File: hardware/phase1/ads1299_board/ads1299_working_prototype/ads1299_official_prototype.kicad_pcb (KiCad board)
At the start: 4 copper layers, 98 parts, among them Con1-32 PinSocket_2x16_P2.54mm_Vertic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, J3 TSM-110-01-T-DV-P-TR, J6 36PIN_IDC, U1 ADS1299IPAG, U10 24AA256-I/ST, U11 SOIC127P599X175-8N, U4 OPA376

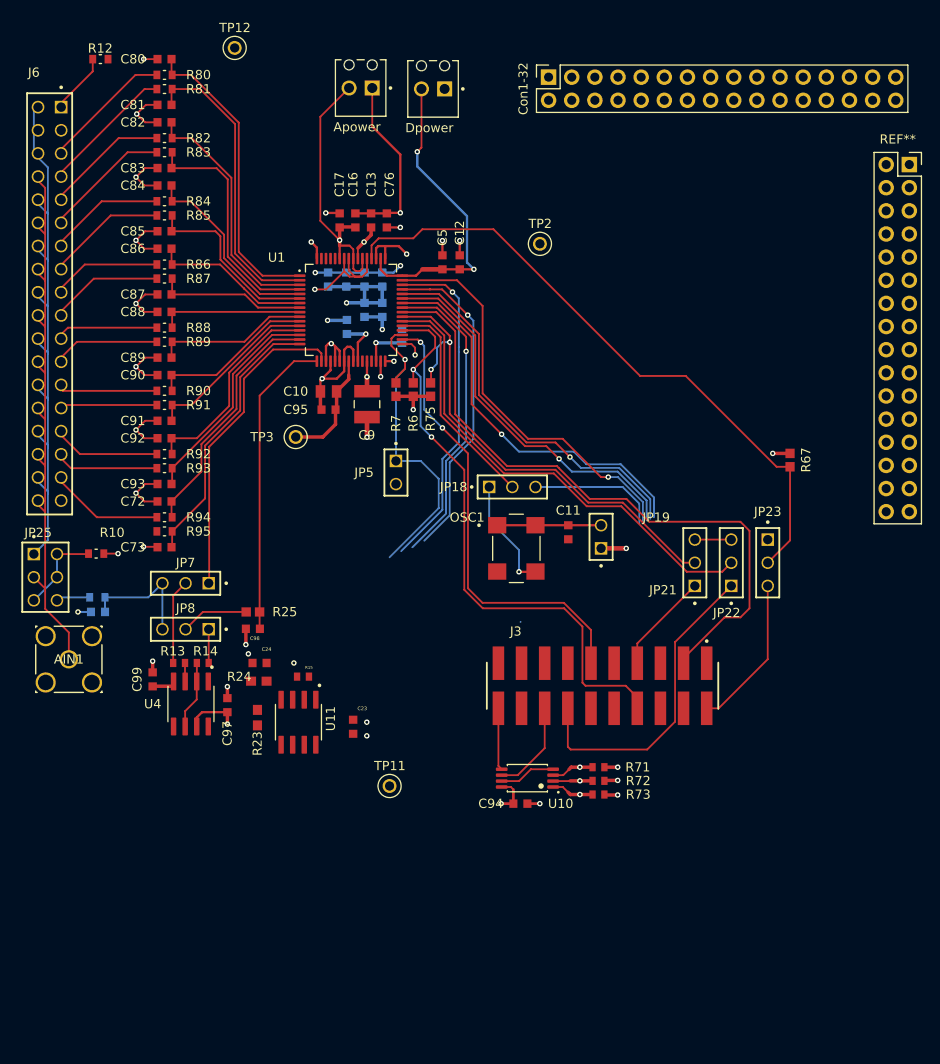
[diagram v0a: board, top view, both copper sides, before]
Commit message: Schematic and Layout updates
Added Bias stuff, routing now and updates from Schematic to Layout working beautifully now. trying to figure out if the capacitors are currently hooked up correctly for AVSS and AVDD or if we need more, not sure if the eval is following a unipolar or bipolar setup
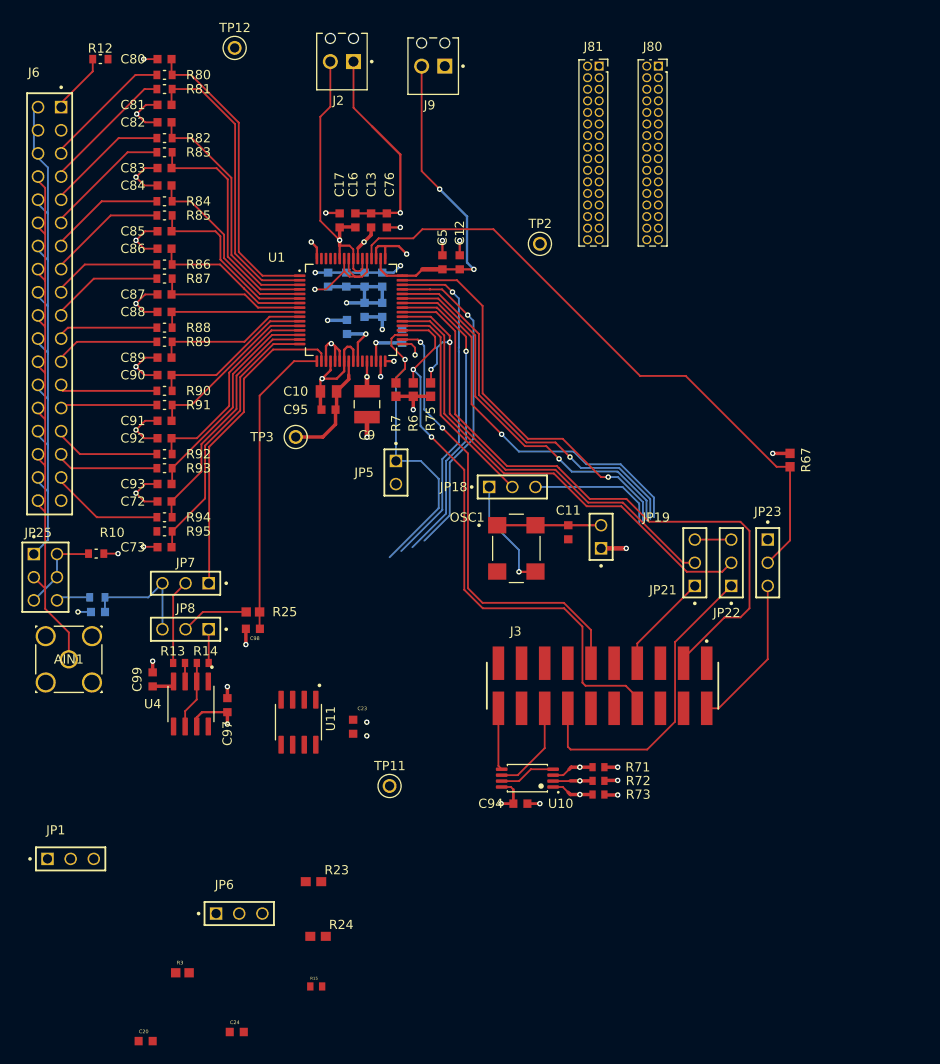
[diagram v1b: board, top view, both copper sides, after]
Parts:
- removed Apower, Dpower: PHOENIX_1725656, 1725656:PHOENIX_1725656
- removed Con1-32, REF**: PinSocket_2x16_P2.54mm_Vertical, Connector_PinSocket_2.54mm:PinSocket_2x16_P2.54mm_Vertical
- added C20: 0.01uF, GRM188R71H103KA01D:CAPC1608X90N, F.Cu at (113.2, 155.0)
- added J2: 1725656, 1725656:PHOENIX_1725656, F.Cu at (137.5, 44.4)
- added J80: Conn_02x16_Odd_Even, Connector_PinSocket_1.27mm:PinSocket_2x16_P1.27mm_Vertical, F.Cu at (169.5, 48.0)
- added J81: Conn_02x16_Odd_Even, Connector_PinSocket_1.27mm:PinSocket_2x16_P1.27mm_Vertical, F.Cu at (163.0, 48.0)
- added J9: 1725656, 1725656:PHOENIX_1725656, F.Cu at (147.6, 44.9)
- added JP1: TSW-103-07-T-S, TSW-103-07-T-S:SAMTEC_TSW-103-07-T-S, F.Cu at (105.0, 135.0)
- added JP6: TSW-103-07-T-S, TSW-103-07-T-S:SAMTEC_TSW-103-07-T-S, F.Cu at (123.5, 141.0)
- added R3: 0, RC0603JR-070RL:RESC1607X60N, F.Cu at (117.3, 147.5)
- C23, C24: value CAPC1608X90N -> 1uF
- R15: value RESC1005X40 -> 0
- R23, R24: value 0603 -> 0
- U11: value SOIC127P599X175-8N -> OPA376AID
- moved C24 40.6 mm to (123.2, 154.0)
- moved R15 34.0 mm to (131.9, 149.0)
- moved R24 28.7 mm to (132.2, 143.5)
- moved R23 19.0 mm to (131.7, 137.5), turned to 0 degrees
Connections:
- C23 pad 1: (no net) -> AVDD
- C23 pad 2: (no net) -> GNDA
- C24 pad 1: (no net) -> AVSS
- C24 pad 2: (no net) -> GNDA
- C99 pad 1: Net-(U4-V-) -> AVSS
- R15 pad 1: (no net) -> Net-(U11--IN)
- R15 pad 2: (no net) -> Net-(JP6-Pad02)
- R23 pad 1: (no net) -> Net-(U11-+IN)
- R23 pad 2: (no net) -> AVDD
- R24 pad 1: (no net) -> AVSS
- R24 pad 2: (no net) -> Net-(U11-+IN)
- U1 pad 17: unconnected-(U1-SRB1-Pad17) -> SRB2
- U1 pad 18: unconnected-(U1-SRB2-Pad18) -> SRB1
- U1 pad 60: unconnected-(U1-BIASREF-Pad60) -> BIASREF
- U1 pad 61: unconnected-(U1-BIASINV-Pad61) -> BIASINV
- U1 pad 62: unconnected-(U1-BIASIN-Pad62) -> BIASIN
- U1 pad 63: unconnected-(U1-BIASOUT-Pad63) -> BIASOUT
- U11 pad 2: (no net) -> Net-(U11--IN)
- U11 pad 3: (no net) -> Net-(U11-+IN)
- U11 pad 4: (no net) -> AVSS
- U11 pad 6: (no net) -> Net-(U11--IN)
- U11 pad 7: (no net) -> AVDD
- U4 pad 4: Net-(U4-V-) -> AVSS
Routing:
- net AVSS: track 61.2 -> 65.0 mm
- net DVDD: track 44.6 -> 46.7 mm
- net AVDD: track 55.9 -> 58.0 mm
- net GNDA: vias 27 -> 25
